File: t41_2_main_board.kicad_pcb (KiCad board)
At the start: 2 copper layers, 100 x 100 mm, 3 parts, among them U1 Teensy4.1

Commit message: Schematic nearing completion.
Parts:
- added IC1: 74HC125D, Package_SO:SOIC-14_3.9x8.7mm_P1.27mm, F.Cu at (168.6, 133.5)
- added J1: Conn_02x08_Odd_Even, Connector_IDC:IDC-Header_2x08_P2.54mm_Vertical, F.Cu at (131.8, 53.5)
- added J2: Conn_02x05_Odd_Even, Connector_IDC:IDC-Header_2x05_P2.54mm_Vertical, F.Cu at (47.5, 63.6)
- added J3: Conn_02x05_Odd_Even, Connector_IDC:IDC-Header_2x05_P2.54mm_Vertical, F.Cu at (59.5, 63.6)
- added J4: Conn_02x05_Odd_Even, Connector_IDC:IDC-Header_2x05_P2.54mm_Vertical, F.Cu at (71.5, 63.6)
- added J5: Conn_02x05_Odd_Even, Connector_IDC:IDC-Header_2x05_P2.54mm_Vertical, F.Cu at (167.3, 146.2)
- added J6: SJ-3524-SMT, Connector_Audio:Jack_3.5mm_CUI_SJ-3524-SMT_Horizontal, F.Cu at (-34.5, 46.2)
- added J7: SJ-3524-SMT, Connector_Audio:Jack_3.5mm_CUI_SJ-3524-SMT_Horizontal, F.Cu at (-22.2, 46.2)
- added J8: SJ-3524-SMT, Connector_Audio:Jack_3.5mm_CUI_SJ-3524-SMT_Horizontal, F.Cu at (-9.97, 46.2)

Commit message: Placement done.
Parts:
- added C1: 0.1uF, Capacitor_SMD:C_1206_3216Metric, F.Cu at (190.4, 95.8)
- added C10: 470pF, Capacitor_SMD:C_1206_3216Metric, F.Cu at (114.2, 117.2)
- added C11: 470pF, Capacitor_SMD:C_1206_3216Metric, B.Cu at (121.7, 112.7)
- added C12: 470pF, Capacitor_SMD:C_1206_3216Metric, F.Cu at (118.7, 95.8)
- added C13: 470pF, Capacitor_SMD:C_1206_3216Metric, B.Cu at (121.6, 102.0)
- added C15: 470pF, Capacitor_SMD:C_1206_3216Metric, B.Cu at (104.1, 96.9)
- added C16: 470pF, Capacitor_SMD:C_1206_3216Metric, F.Cu at (157.8, 140.0)
- added C2: 10uF, Capacitor_SMD:C_1206_3216Metric, F.Cu at (193.7, 120.8)
- added C3: 470pF, Capacitor_SMD:C_1206_3216Metric, F.Cu at (192.5, 92.1)
- added C4: 0.1uF, Capacitor_SMD:C_1206_3216Metric, F.Cu at (115.0, 124.1)
- added C5: 0.1uF, Capacitor_SMD:C_1206_3216Metric, F.Cu at (115.0, 129.6)
- added C6: 0.1uF, Capacitor_SMD:C_1206_3216Metric, F.Cu at (115.0, 137.5)
- added C7: 470pF, Capacitor_SMD:C_1206_3216Metric, F.Cu at (121.7, 90.1)
- added C8: 470pF, Capacitor_SMD:C_1206_3216Metric, F.Cu at (121.6, 86.8)
- added C9: 470pF, Capacitor_SMD:C_1206_3216Metric, F.Cu at (183.6, 145.4)
- added FB1: FerriteBead, Inductor_SMD:L_1206_3216Metric, F.Cu at (110.2, 125.9)
- added FB10: FerriteBead, Inductor_SMD:L_1206_3216Metric, B.Cu at (104.1, 100.5)
- added FB2: FerriteBead, Inductor_SMD:L_1206_3216Metric, F.Cu at (110.2, 130.9)
- added FB3: FerriteBead, Inductor_SMD:L_1206_3216Metric, F.Cu at (110.2, 136.0)
- added FB4: FerriteBead, Inductor_SMD:L_1206_3216Metric, F.Cu at (115.5, 90.1)
- added FB5: FerriteBead, Inductor_SMD:L_1206_3216Metric, F.Cu at (115.6, 86.8)
- added FB6: FerriteBead, Inductor_SMD:L_1206_3216Metric, F.Cu at (114.3, 113.9)
- added FB7: FerriteBead, Inductor_SMD:L_1206_3216Metric, B.Cu at (121.6, 109.4)
- added FB8: FerriteBead, Inductor_SMD:L_1206_3216Metric, F.Cu at (115.7, 98.9)
- added FB9: FerriteBead, Inductor_SMD:L_1206_3216Metric, B.Cu at (121.5, 105.5)
- added J10: SJ-3524-SMT, SJ-3524-SMT:CUI_SJ-3524-SMT, F.Cu at (100.6, 94.1)
- added J11: B2B-XH-A_LF__SN_, digikey-footprints:PinHeader_1x2_P2.5mm_Drill1.1mm, F.Cu at (117.9, 79.9)
- added J12: SJ-3524-SMT, SJ-3524-SMT:CUI_SJ-3524-SMT, F.Cu at (184.4, 137.3)
- added J13: B3B-XH-A_LF__SN_, digikey-footprints:PinHeader_1x3_P2.5mm_Drill1.1mm, B.Cu at (193.7, 88.5)
- added J15: B4B-XH-A_LF__SN_, digikey-footprints:PinHeader_1x4_P2.5mm_Drill1.1mm, F.Cu at (163.9, 140.0)
- added J9: B3B-XH-A_LF__SN_, digikey-footprints:PinHeader_1x3_P2.5mm_Drill1.1mm, F.Cu at (118.4, 73.0)
- added R2: 100, Resistor_SMD:R_1206_3216Metric, F.Cu at (143.2, 77.3)
- added R3: 100, Resistor_SMD:R_1206_3216Metric, F.Cu at (146.5, 77.3)
- added R4: 100, Resistor_SMD:R_1206_3216Metric, F.Cu at (138.1, 77.3)
- J2, J3, J4, J5: moved to B.Cu
- J6, J7, J8: footprint Connector_Audio:Jack_3.5mm_CUI_SJ-3524-SMT_Horizontal -> SJ-3524-SMT:CUI_SJ-3524-SMT
- moved J6 135.8 mm to (100.6, 59.8)
- moved J2 132.6 mm to (180.0, 57.3), turned to -90 degrees
- moved J7 125.4 mm to (100.6, 71.3)
- moved J8 116.4 mm to (100.6, 82.7)
- moved J4 87.1 mm to (158.4, 57.3), turned to -90 degrees
- moved J1 74.4 mm to (100.0, 120.8), turned to 0 degrees
- moved J5 70.5 mm to (190.2, 79.5), turned to 0 degrees
- moved J3 69.3 mm to (112.7, 108.1), turned to 90 degrees
- moved U1 39.2 mm to (161.0, 120.8), turned to 0 degrees
- moved IC1 37.1 mm to (189.5, 102.9), turned to 180 degrees
- moved U3 34.4 mm to (173.7, 84.0), turned to 0 degrees
- moved U2 33.0 mm to (144.4, 85.2), turned to 90 degrees
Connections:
- net Net-(J5-Pin_3) renamed /CLK0_OUT
- IC1 pad 1: unconnected-(IC1-Pad1) -> /CS
- IC1 pad 10: unconnected-(IC1-Pad10) -> /CS
- IC1 pad 14: unconnected-(IC1-Pad14) -> /3_3V_FIL
- IC1 pad 2: unconnected-(IC1-Pad2) -> /MOSI
- IC1 pad 3: /MOSI -> /MOSI_OUT
- IC1 pad 4: unconnected-(IC1-Pad4) -> /CS
- IC1 pad 5: unconnected-(IC1-Pad5) -> /MISO_IN
- IC1 pad 6: unconnected-(IC1-Pad6) -> /MISO
- IC1 pad 9: unconnected-(IC1-Pad9) -> /CLK0
- J1 pad 1: unconnected-(J1-Pin_1-Pad1) -> /RESET
- J1 pad 10: unconnected-(J1-Pin_10-Pad10) -> /5V_IN
- J1 pad 13: /3_3V -> /3_3V_IN
- J1 pad 14: /3_3V -> /3_3V_IN
- J1 pad 2: unconnected-(J1-Pin_2-Pad2) -> /TXRX
- J1 pad 3: unconnected-(J1-Pin_3-Pad3) -> /SDA
- J1 pad 4: unconnected-(J1-Pin_4-Pad4) -> /SCL
- J1 pad 5: unconnected-(J1-Pin_5-Pad5) -> /12V_IN
- J1 pad 6: unconnected-(J1-Pin_6-Pad6) -> /12V_IN
- J1 pad 9: unconnected-(J1-Pin_9-Pad9) -> /5V_IN
- J2 pad 1: unconnected-(J2-Pin_1-Pad1) -> GND
- J2 pad 2: unconnected-(J2-Pin_2-Pad2) -> GND
- J2 pad 5: unconnected-(J2-Pin_5-Pad5) -> Net-(J2-Pin_5)
- J2 pad 6: unconnected-(J2-Pin_6-Pad6) -> Net-(J2-Pin_6)
- J2 pad 7: unconnected-(J2-Pin_7-Pad7) -> Net-(J2-Pin_7)
- J2 pad 8: unconnected-(J2-Pin_8-Pad8) -> Net-(J2-Pin_8)
- J3 pad 1: unconnected-(J3-Pin_1-Pad1) -> Net-(J3-Pin_1)
- J3 pad 10: unconnected-(J3-Pin_10-Pad10) -> Net-(J3-Pin_10)
- J3 pad 2: unconnected-(J3-Pin_2-Pad2) -> Net-(J3-Pin_2)
- J3 pad 3: unconnected-(J3-Pin_3-Pad3) -> Net-(J3-Pin_3)
- J3 pad 4: unconnected-(J3-Pin_4-Pad4) -> Net-(J3-Pin_4)
- J3 pad 7: unconnected-(J3-Pin_7-Pad7) -> /SDA
- J3 pad 8: unconnected-(J3-Pin_8-Pad8) -> /SCL
- J3 pad 9: unconnected-(J3-Pin_9-Pad9) -> GND
- J4 pad 1: unconnected-(J4-Pin_1-Pad1) -> GND
- J4 pad 2: unconnected-(J4-Pin_2-Pad2) -> GND
- J4 pad 5: unconnected-(J4-Pin_5-Pad5) -> Net-(J4-Pin_5)
- J4 pad 6: unconnected-(J4-Pin_6-Pad6) -> Net-(J4-Pin_6)
- J4 pad 7: unconnected-(J4-Pin_7-Pad7) -> Net-(J4-Pin_7)
- J4 pad 8: unconnected-(J4-Pin_8-Pad8) -> Net-(J4-Pin_8)
- J5 pad 4: /MOSI -> /MOSI_OUT
- J5 pad 5: /MISO -> /MISO_IN
- U1 pad 12: unconnected-(U1-10_CS_MQSR-Pad12) -> /CS
- U1 pad 13: unconnected-(U1-11_MOSI_CTX1-Pad13) -> /MOSI
- U1 pad 14: unconnected-(U1-12_MISO_MQSL-Pad14) -> /MISO
- U1 pad 2: unconnected-(U1-0_RX1_CRX2_CS1-Pad2) -> /RESET
- U1 pad 20: unconnected-(U1-28_RX7-Pad20) -> /20MFILTER
- U1 pad 21: unconnected-(U1-29_TX7-Pad21) -> /15MFILTER
- U1 pad 22: unconnected-(U1-30_CRX3-Pad22) -> /80MFILTER
- U1 pad 23: unconnected-(U1-31_CTX3-Pad23) -> /40MFILTER
- U1 pad 24: unconnected-(U1-32_OUT1B-Pad24) -> /DIN
- U1 pad 27: unconnected-(U1-35_TX8-Pad27) -> /KEY2
- U1 pad 28: unconnected-(U1-36_CS-Pad28) -> /KEY1
- U1 pad 29: unconnected-(U1-37_CS-Pad29) -> /PTT
- U1 pad 30: unconnected-(U1-38_CS1_IN1-Pad30) -> /MUTE
- U1 pad 31: unconnected-(U1-39_MISO1_OUT1A-Pad31) -> /SWITCH_MATRIX
- U1 pad 34: unconnected-(U1-GND-Pad34) -> GND
- U1 pad 35: unconnected-(U1-13_SCK_LED-Pad35) -> /CLK0
- U1 pad 36: unconnected-(U1-14_A0_TX3_SPDIF_OUT-Pad36) -> Net-(J4-Pin_6)
- U1 pad 37: unconnected-(U1-15_A1_RX3_SPDIF_IN-Pad37) -> Net-(J4-Pin_8)
- U1 pad 38: unconnected-(U1-16_A2_RX4_SCL1-Pad38) -> Net-(J4-Pin_5)
- U1 pad 39: unconnected-(U1-17_A3_TX4_SDA1-Pad39) -> Net-(J4-Pin_7)
- U1 pad 4: unconnected-(U1-2_OUT2-Pad4) -> Net-(J2-Pin_5)
- U1 pad 40: unconnected-(U1-18_A4_SDA-Pad40) -> /SDA
- U1 pad 41: unconnected-(U1-19_A5_SCL-Pad41) -> /SCL
- U1 pad 42: unconnected-(U1-20_A6_TX5_LRCLK1-Pad42) -> /LRCLK
- U1 pad 43: unconnected-(U1-21_A7_RX5_BCLK1-Pad43) -> /BCK
- U1 pad 44: unconnected-(U1-22_A8_CTX1-Pad44) -> /TXRX
- U1 pad 45: unconnected-(U1-23_A9_CRX1_MCLK1-Pad45) -> /MCLK
- U1 pad 46: unconnected-(U1-3V3-Pad46) -> /3V3
- U1 pad 47: unconnected-(U1-GND-Pad47) -> GND
- U1 pad 48: unconnected-(U1-VIN-Pad48) -> /5V_FIL
- U1 pad 5: unconnected-(U1-3_LRCLK2-Pad5) -> Net-(J2-Pin_7)
- U1 pad 6: unconnected-(U1-4_BCLK2-Pad6) -> Net-(J2-Pin_6)
- U1 pad 7: unconnected-(U1-5_IN2-Pad7) -> Net-(J2-Pin_8)
- U1 pad 8: unconnected-(U1-6_OUT1D-Pad8) -> /OUT
- U2 pad 11: unconnected-(U2-OUT-Pad11) -> /OUT
- U2 pad 14: Net-(J6-Pad1) -> GND
- U2 pad 5: /3_3V -> /3_3V_FIL
- U2 pad 6: /5V -> /5V_FIL
- U2 pad 7: /3_3V -> /3_3V_FIL
- U3 pad 11: unconnected-(U3-BCK-Pad11) -> /BCK
- U3 pad 12: unconnected-(U3-DIN-Pad12) -> /DIN
- U3 pad 13: unconnected-(U3-LRCK-Pad13) -> /LRCLK
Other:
- outline, holes or cut-outs redrawn

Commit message: Closing in on finished layout.
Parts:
- moved C9 19.4 mm to (167.4, 134.8)
- moved J12 7.04 mm to (191.5, 137.3), turned to 180 degrees
- moved C1 3.26 mm to (187.2, 96.0)
- moved C7 2.07 mm to (120.2, 91.5), turned to 90 degrees
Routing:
- net /3_3V_FIL: track 0.00 -> 156.6 mm, vias 0 -> 1
- net Net-(J2-Pin_5): track 0.00 -> 118.5 mm
- net /CS: track 0.00 -> 102.5 mm
- net Net-(J2-Pin_7): track 0.00 -> 101.0 mm
- net Net-(J2-Pin_8): track 0.00 -> 92.2 mm
- net Net-(J2-Pin_6): track 0.00 -> 92.1 mm
- net /PTT: track 0.00 -> 90.2 mm
- net /40MFILTER: track 0.00 -> 86.1 mm
- net /15MFILTER: track 0.00 -> 83.1 mm
- net /80MFILTER: track 0.00 -> 80.9 mm
- net /BCK: track 0.00 -> 79.7 mm, vias 0 -> 1
- net /KEY2: track 0.00 -> 79.1 mm
- net /SDA: track 0.00 -> 78.8 mm
- net /KEY1: track 0.00 -> 77.3 mm
- net /LRCLK: track 0.00 -> 71.9 mm, vias 0 -> 1
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- added copper zone on B.Cu, net GND
- added copper zone on F.Cu, net GND

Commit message: Branching here to alternative layout.
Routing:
- net Net-(U3-LROUT): track 27.9 -> 30.0 mm
- net /DIN: track 64.8 -> 66.2 mm
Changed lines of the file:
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@@
 		(at 191.483 137.3 180)
 		(property "Reference" "J12"
-			(at 0.075115 -5.945065 360)
+			(at 0.075115 -5.945065 0)
 			(layer "F.SilkS")
 			(effects
@@
 		)
 		(property "Value" "SJ-3524-SMT"
-			(at 6.33435 5.97385 360)
+			(at 6.33435 5.97385 0)
 			(layer "F.Fab")
 			(hide yes)
@@
 		)
 		(property "Footprint" "SJ-3524-SMT:CUI_SJ-3524-SMT"
-			(at 0 0 360)
+			(at 0 0 0)
 			(layer "F.Fab")
 			(hide yes)
@@
 		)
 		(property "Datasheet" ""
-			(at 0 0 360)
+			(at 0 0 0)
 			(layer "F.Fab")
 			(hide yes)
@@
 		)
 		(property "Description" ""
-			(at 0 0 360)
+			(at 0 0 0)
 			(layer "F.Fab")
 			(hide yes)
@@
 	)
 	(via
-		(at 181.4324 109.8934)
+		(at 180.4418 110.3252)
 		(size 1)
 		(drill 0.5)
@@
 	)
 	(segment
-		(start 175.121 101.1134)
-		(end 177.2208 103.2132)
-		(width 0.25)
+		(start 181.7118 109.2076)
+		(end 183.2104 110.7062)
+		(width 0.2)
 		(layer "F.Cu")
 		(net 85)
 	)
 	(segment
-		(start 186.36 124.6)
+		(start 175.184 76.6956)
+		(end 175.184 103.7466)
+		(width 0.2)
+		(layer "F.Cu")
+		(net 85)
+	)
+	(segment
+		(start 184.6502 110.7062)
 		(end 186.36 112.416)
 		(width 0.2)
@@
 	)
 	(segment
-		(start 177.2208 103.2768)
-		(end 177.2208 103.2132)
+		(start 186.36 124.6)
+		(end 190.17 128.41)
 		(width 0.2)
 		(layer "F.Cu")
@@
 	)
 	(segment
-		(start 175.184 76.6956)
-		(end 175.121 76.7586)
-		(width 0.25)
+		(start 175.184 103.7466)
+		(end 180.645 109.2076)
+		(width 0.2)
 		(layer "F.Cu")
 		(net 85)
 	)
 	(segment
-		(start 186.36 112.416)
-		(end 177.2208 103.2768)
+		(start 183.2104 110.7062)
+		(end 184.6502 110.7062)
 		(width 0.2)
 		(layer "F.Cu")
@@
 	)
 	(segment
-		(start 190.17 128.41)
+		(start 186.36 112.416)
 		(end 186.36 124.6)
 		(width 0.2)
@@
 	)
 	(segment
-		(start 175.121 76.7586)
-		(end 175.121 101.1134)
-		(width 0.25)
+		(start 180.645 109.2076)
+		(end 181.7118 109.2076)
+		(width 0.2)
 		(layer "F.Cu")
 		(net 85)
@@
 	)
 	(segment
-		(start 188.9 111.6997)
-		(end 181.28 104.0797)
+		(start 183.5152 109.8934)
+		(end 185.1916 109.8934)
 		(width 0.2)
 		(layer "F.Cu")
@@
 	)
 	(segment
-		(start 188.9 114.538)
+		(start 188.0589 110.8586)
 		(end 188.9 111.6997)
 		(width 0.2)
@@
 	)
 	(segment
-		(start 181.28 104.0797)
-		(end 181.28 96.66)
+		(start 181.28 107.6582)
+		(end 183.5152 109.8934)
 		(width 0.2)
 		(layer "F.Cu")
@@
 	)
 	(segment
-		(start 193.726 119.364)
+		(start 188.9 111.6997)
 		(end 188.9 114.538)
 		(width 0.2)
 		(layer "F.Cu")
+		(net 115)
+	)
+	(segment
+		(start 188.9 114.538)
+		(end 193.726 119.364)
+		(width 0.2)
+		(layer "F.Cu")
+		(net 115)
+	)
+	(segment
+		(start 181.28 96.66)
+		(end 181.28 107.6582)
+		(width 0.2)
+		(layer "F.Cu")
+		(net 115)
+	)
+	(segment
+		(start 186.1568 110.8586)
+		(end 188.0589 110.8586)
+		(width 0.2)
+		(layer "F.Cu")
+		(net 115)
+	)
+	(segment
+		(start 185.1916 109.8934)
+		(end 186.1568 110.8586)
+		(width 0.2)
+		(layer "F.Cu")

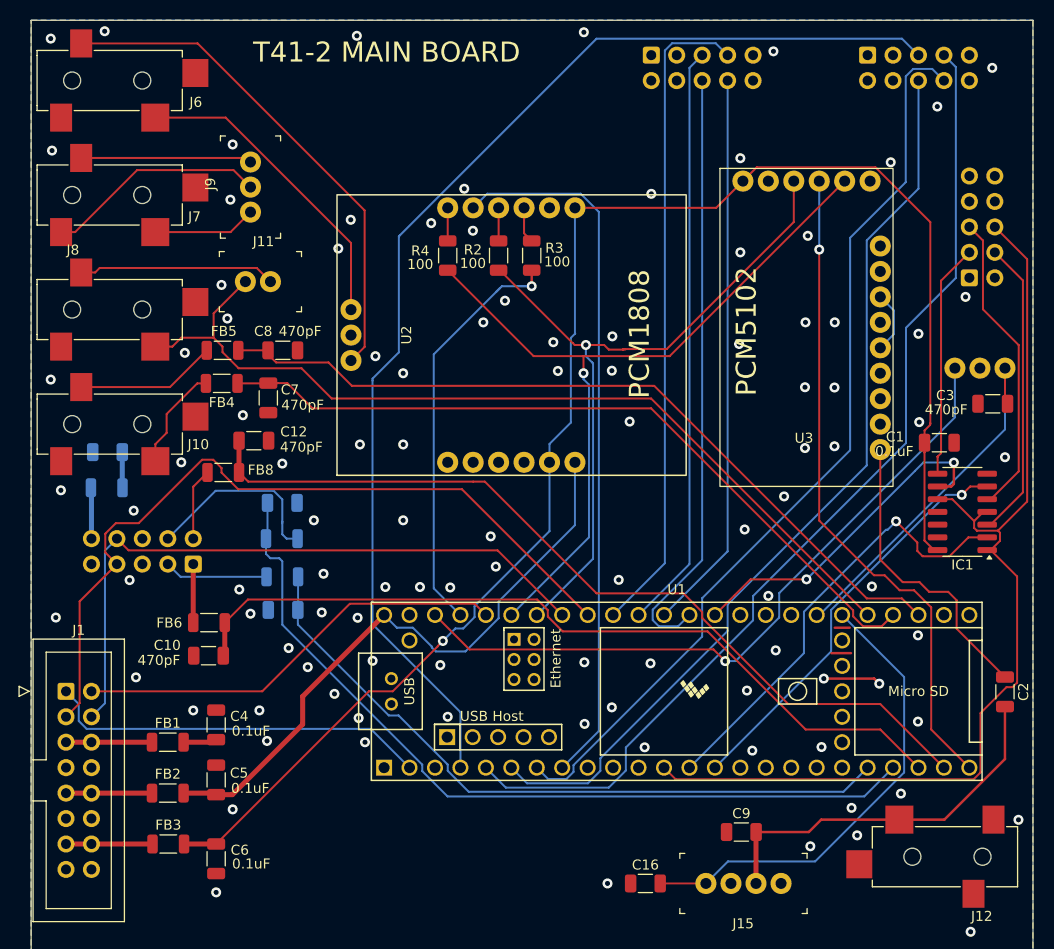
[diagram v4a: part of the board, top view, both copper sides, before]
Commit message: Audio routing is not good, starting another branch.
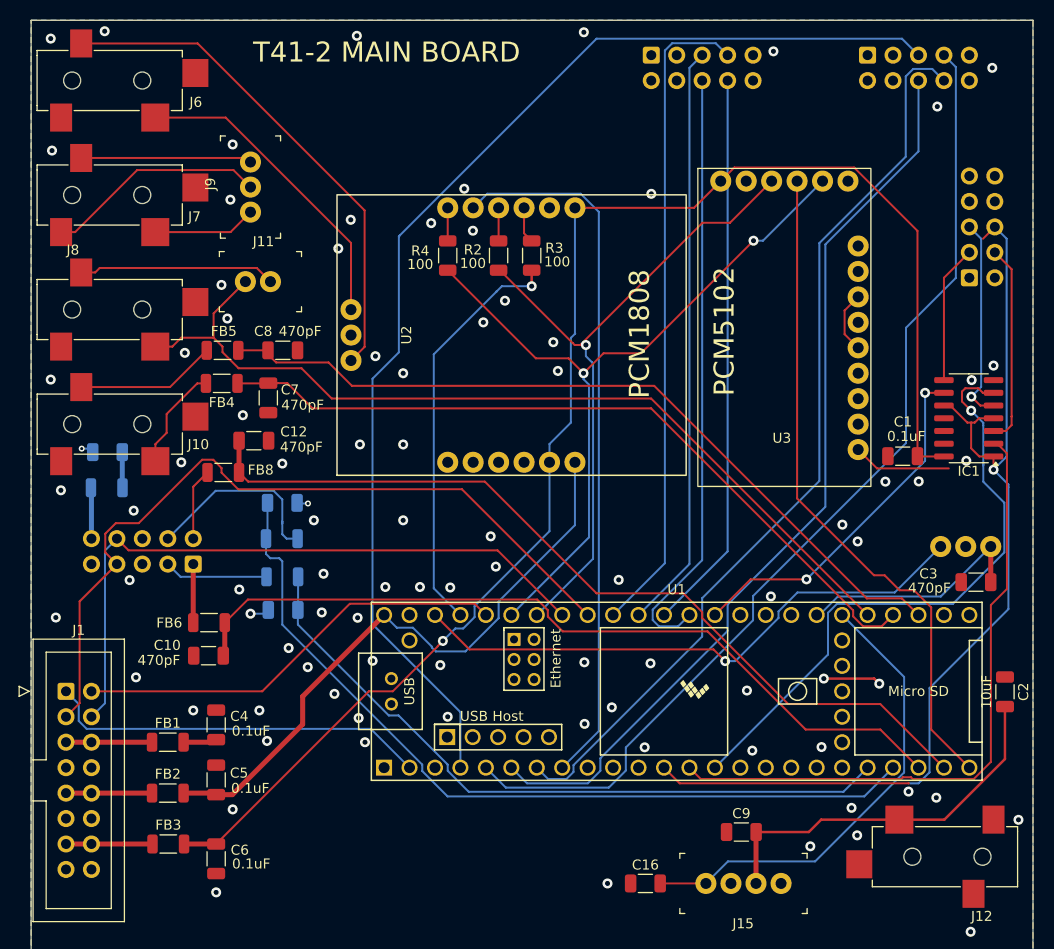
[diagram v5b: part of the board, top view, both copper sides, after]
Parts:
- moved C3 17.9 mm to (190.8, 109.9)
- moved J13 17.9 mm to (192.3, 106.3)
- moved IC1 9.37 mm to (190.1, 93.5)
- moved C1 3.90 mm to (183.5, 97.3), turned to 180 degrees
- moved U3 2.21 mm to (171.5, 84.0)
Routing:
- net /MISO: track 41.2 -> 61.8 mm
- net Net-(U3-LROUT): track 30.0 -> 9.82 mm
- net /MOSI: track 45.0 -> 64.6 mm, vias 1 -> 0
- net /3V3: track 70.2 -> 57.5 mm
- net /SWITCH_MATRIX: track 36.2 -> 24.2 mm
- net /MISO_IN: track 30.7 -> 20.4 mm, vias 0 -> 1
- net /MOSI_OUT: track 30.0 -> 20.0 mm
- net /CLK0_OUT: track 23.4 -> 13.8 mm
- net /3_3V_FIL: track 156.6 -> 147.0 mm
- net /LRCLK: track 71.9 -> 67.3 mm
- net GND: track 5.75 -> 10.0 mm, vias 104 -> 89
- net (no net): track 3.45 -> 0.00 mm
- net /BCK: track 79.7 -> 77.2 mm, vias 1 -> 2
- net /CLK0: track 34.0 -> 36.0 mm
- net /MCLK: track 43.2 -> 41.3 mm
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
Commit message: This new layout is excellent.
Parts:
- moved C2 45.3 mm to (149.2, 129.2), turned to 180 degrees
- moved U3 38.5 mm to (143.1, 110.0)
- moved U1 23.5 mm to (167.4, 98.1), turned to 90 degrees
- moved J15 21.8 mm to (142.7, 134.8)
- moved C9 19.9 mm to (185.9, 127.3), turned to 180 degrees
- moved C16 13.6 mm to (144.2, 139.6), turned to 180 degrees
- moved U2 13.2 mm to (138.0, 73.7), turned to 0 degrees
- moved R4 12.7 mm to (146.0, 67.3), turned to 180 degrees
- moved R2 5.90 mm to (146.0, 72.1), turned to 180 degrees
- moved J12 2.78 mm to (192.8, 134.8)
- moved R3 1.95 mm to (146.0, 75.4), turned to 180 degrees
- moved C1 1.53 mm to (183.6, 98.8), turned to -90 degrees
- moved IC1 1.07 mm to (189.0, 93.6)
- moved C8 0.61 mm to (121.0, 86.8)
- moved J11 0.36 mm to (117.6, 79.9)
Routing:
- net /5V_FIL: track 62.2 -> 118.1 mm
- net Net-(J2-Pin_5): track 118.5 -> 67.9 mm
- net /SWITCH_MATRIX: track 24.2 -> 74.5 mm, vias 0 -> 1
- net /RESET: track 38.4 -> 87.0 mm
- net /CS: track 100.8 -> 52.7 mm, vias 2 -> 0
- net /3_3V_FIL: track 147.0 -> 195.2 mm, vias 1 -> 0
- net /MOSI: track 64.6 -> 17.4 mm
- net /MUTE: track 47.2 -> 93.3 mm, vias 0 -> 1
- net /MISO: track 61.8 -> 17.9 mm, vias 1 -> 0
- net Net-(J2-Pin_7): track 101.0 -> 65.1 mm
- net Net-(J2-Pin_6): track 92.1 -> 59.0 mm
- net /20MFILTER: track 69.9 -> 102.4 mm
- net /15MFILTER: track 83.1 -> 114.1 mm
- net /KEY2: track 79.1 -> 48.5 mm
- net /PTT: track 90.2 -> 63.0 mm
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
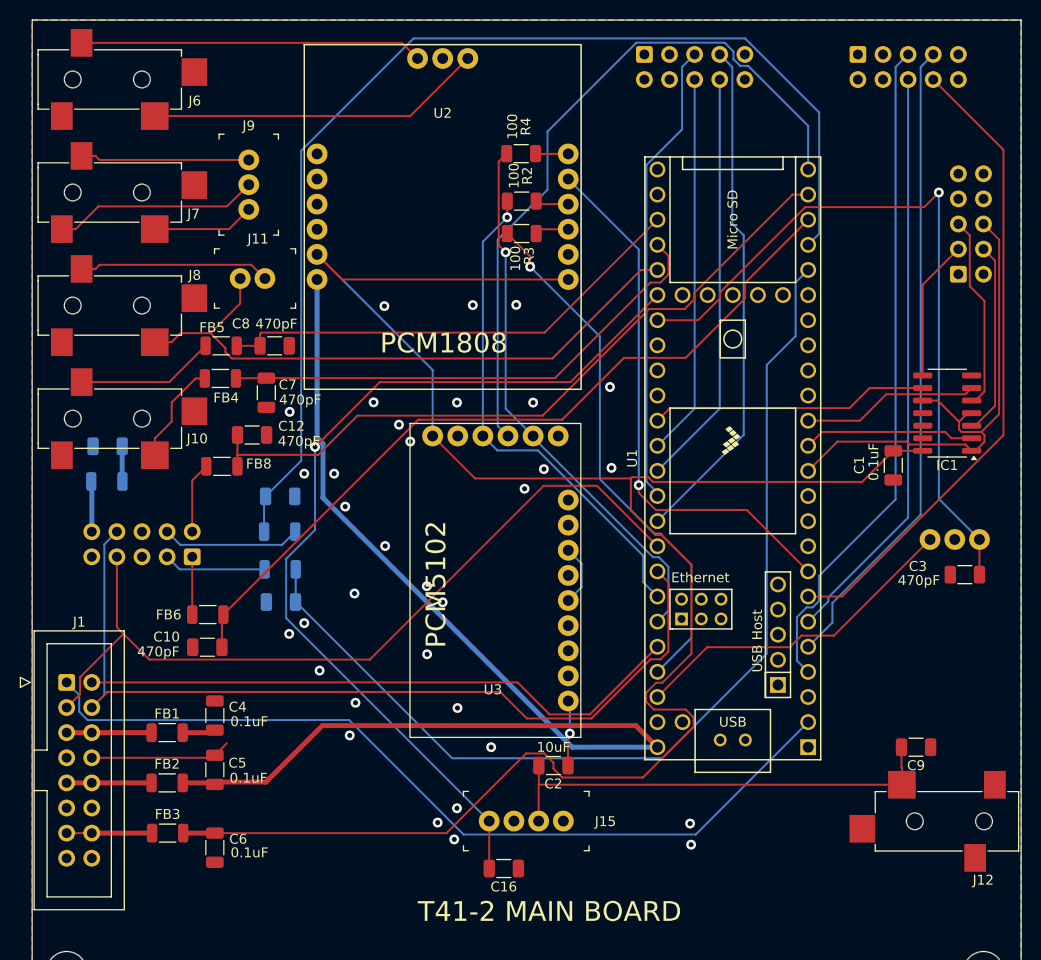
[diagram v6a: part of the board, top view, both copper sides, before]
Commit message: Branching prior to adding SPDIF.
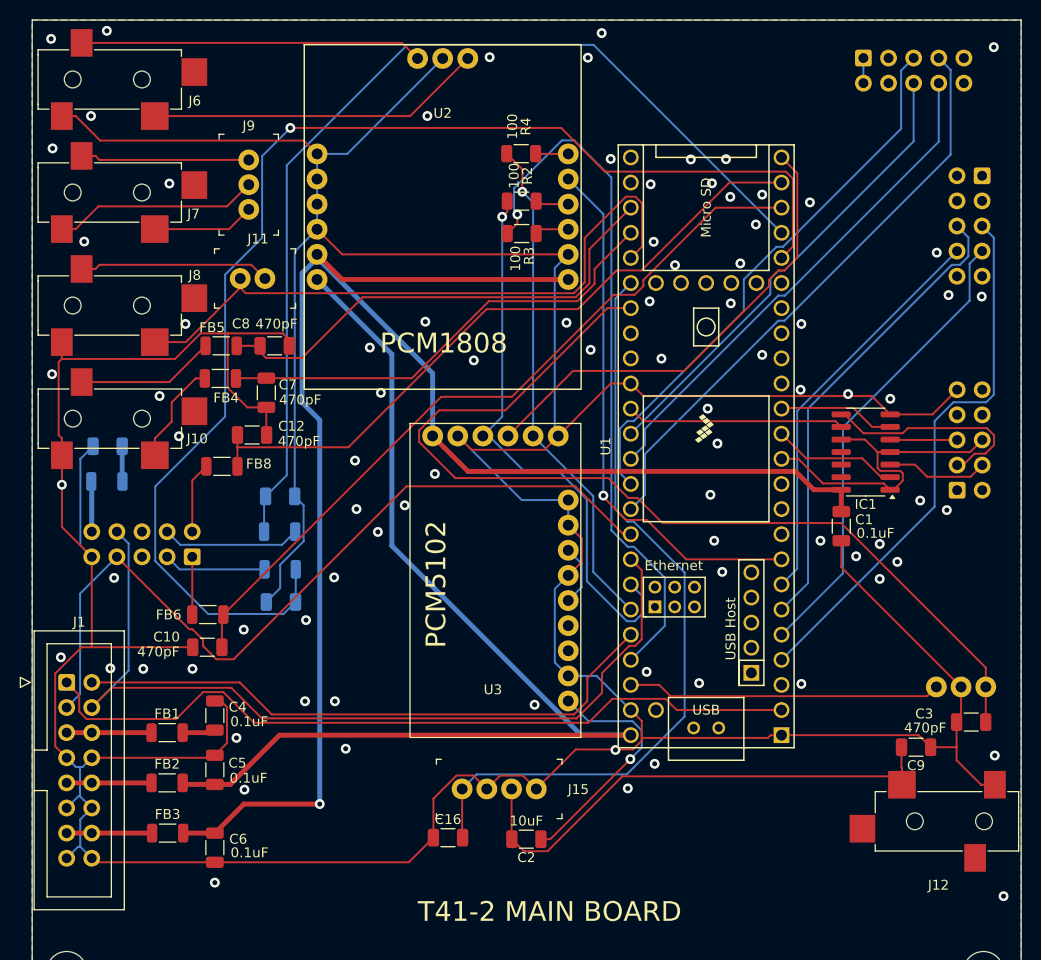
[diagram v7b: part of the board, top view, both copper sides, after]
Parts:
- moved J4 22.2 mm to (180.6, 57.7)
- moved J5 21.8 mm to (190.0, 101.4)
- moved J2 17.6 mm to (192.6, 69.6), turned to 180 degrees
- moved J13 14.9 mm to (192.9, 121.2)
- moved C3 14.9 mm to (191.5, 124.8)
- moved IC1 9.14 mm to (180.8, 97.5)
- moved C1 8.09 mm to (178.3, 105.0)
- moved C2 7.93 mm to (146.5, 136.6)
- moved C16 6.45 mm to (138.6, 136.5), turned to 0 degrees
- moved J15 4.25 mm to (140.0, 131.6)
- moved U1 2.96 mm to (164.7, 96.9)
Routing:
- net GND: track 14.9 -> 515.9 mm, vias 33 -> 85
- net /20MFILTER: track 102.4 -> 131.1 mm, vias 0 -> 1
- net /3_3V_FIL: track 195.2 -> 167.0 mm, vias 0 -> 1
- net /SWITCH_MATRIX: track 74.5 -> 100.0 mm, vias 1 -> 0
- net Net-(J2-Pin_8): track 65.4 -> 41.1 mm
- net /DIN: track 71.7 -> 47.9 mm
- net /CS: track 52.7 -> 34.4 mm
- net Net-(J2-Pin_7): track 65.1 -> 47.2 mm
- net Net-(U3-LROUT): track 6.67 -> 24.4 mm
- net /MCLK: track 53.8 -> 71.3 mm
- net /MUTE: track 93.3 -> 78.2 mm, vias 1 -> 0
- net /15MFILTER: track 114.1 -> 100.9 mm
- net /MISO_IN: track 19.7 -> 6.79 mm
- net Net-(J2-Pin_5): track 67.9 -> 55.2 mm
- net Net-(J2-Pin_6): track 59.0 -> 47.6 mm
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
